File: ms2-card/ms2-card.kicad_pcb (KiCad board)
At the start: 2 copper layers, 100 x 54 mm, 40 parts, among them J1 Schaltregler, J10 MicroSD_SPI_CD, J11 I2C, J2 ESP Prog, J20 Smartcard Connector, J21 Card Edge, J23 Conn_01x04, J3 RTS, J30 USB_B_Micro, J31 Power Select, J32 FTDI Adapter, J40 SP1, J50 Conn_01x05, J51 SP1, Q30 BC847, SW1 RESET, U1 ESP-12F, U30 CH330N, U40 ADUM1250, U41 ADuM1201AR

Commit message: wip
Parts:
- removed C1: 100uF, Capacitor_Tantalum_SMD:CP_EIA-7343-31_Kemet-D_Pad2.25x2.55mm_HandSolder
- removed C30, C31, C40, C41, C50, C51: 100nF, Capacitors_SMD:C_0805_HandSoldering
- removed J1: Schaltregler, Connector_PinHeader_2.54mm:PinHeader_1x04_P2.54mm_Vertical
- removed J2: ESP Prog, Connector_PinHeader_2.54mm:PinHeader_1x02_P2.54mm_Vertical
- removed J3: RTS, Connector_PinHeader_2.54mm:PinHeader_1x01_P2.54mm_Vertical
- removed J31: Power Select, Connector_PinHeader_2.54mm:PinHeader_1x03_P2.54mm_Vertical
- removed J32: FTDI Adapter, Connector_PinSocket_2.54mm:PinSocket_1x06_P2.54mm_Horizontal
- removed J40, J51: SP1, Connector_PinHeader_2.54mm:PinHeader_1x01_P2.54mm_Vertical
- removed J50: Conn_01x05, Connector_PinHeader_2.54mm:PinHeader_1x05_P2.54mm_Vertical
- removed R2, R50, R51: 4k7, Resistors_SMD:R_0805_HandSolderingII
- removed U30: CH330N, Package_SO:SOIC-8_3.9x4.9mm_P1.27mm
- removed U40: ADUM1250, Package_SO:SOIC-8_3.9x4.9mm_P1.27mm
- removed U41: ADuM1201AR, Package_SO:SOIC-8_3.9x4.9mm_P1.27mm
- added Brd1: SSD1306, Lokkarten:128x64OLED, F.Cu at (173.4, 114.2)
- added J22: Card Edge, w_conn_misc:MS2_Edge, F.Cu at (104.2, 105.7)
- added M1: PI_PICO_ZERO, Lokkarten:PI_PICO_ZERO, F.Cu at (186.5, 142.6)
- J30: value USB_B_Micro -> Power Only
- R1: value 1k -> 330
- SW1: value RESET -> SW_Push
- U1: value ESP-12F -> W25Q128JVS; footprint ESP8266:ESP-12E -> Package_SO:SOIC-8_5.23x5.23mm_P1.27mm
- moved J11 49.3 mm to (172.8, 151.4), turned to 270 degrees
- moved D1 29.9 mm to (187.2, 130.2), turned to 180 degrees
- moved R1 25.8 mm to (180.7, 130.2)
- moved U1 20.4 mm to (171.0, 111.0), turned to 90 degrees
- moved J23 20.2 mm to (162.2, 133.2)
- moved J30 15.4 mm to (194.9, 127.1)
- moved R22 15.2 mm to (171.5, 131.5), turned to 0 degrees
- moved Q30 14.8 mm to (171.2, 125.3)
- moved R23 14.8 mm to (171.4, 128.7)
- moved R24 14.8 mm to (171.4, 122.1)
- moved R20 13.2 mm to (168.4, 144.4)
- moved R21 13.2 mm to (170.6, 144.4)
- moved SW1 10.1 mm to (167.5, 138.1), turned to 90 degrees
- moved J10 4.26 mm to (183.8, 113.2)
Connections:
- J10 pad 2: /CS -> /CS0
- J30 pad 1: /VBUS -> +5V
- SW1 pad 1: GND -> Net-(SW1-Pad1)
- U1 pad 1: Net-(SW1-Pad2) -> /CS1
- U1 pad 2: Net-(U1-Pad2) -> /MISO
- U1 pad 3: VCC -> Net-(U1-Pad3)
- U1 pad 4: /Card -> GND
- U1 pad 5: /CLK -> /MOSI
- U1 pad 6: /MISO -> /CLK
- U1 pad 7: /MOSI -> Net-(U1-Pad7)
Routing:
- net /SCL: track 155.3 -> 0.00 mm, vias 3 -> 0
- net VCC: track 150.9 -> 0.00 mm, vias 5 -> 0
- net /SDA: track 117.1 -> 0.00 mm, vias 2 -> 0
- net GND: track 89.6 -> 0.00 mm, vias 26 -> 0
- net Net-(J21-Pad1): track 71.5 -> 0.00 mm, vias 1 -> 0
- net /Card: track 69.6 -> 0.00 mm, vias 4 -> 0
- net /MS2PWR: track 62.2 -> 0.00 mm
- net Net-(J20-Pad2): track 61.2 -> 0.00 mm, vias 1 -> 0
- net Net-(J20-Pad4): track 52.8 -> 0.00 mm
- net Net-(J20-Pad7): track 45.8 -> 0.00 mm, vias 1 -> 0
- net /VBUS: track 44.8 -> 0.00 mm, vias 3 -> 0
- net Net-(J20-Pad5): track 44.0 -> 0.00 mm
- net /CS: track 40.3 -> 0.00 mm
- net Net-(SW1-Pad2): track 32.9 -> 0.00 mm
- net /MOSI: track 30.0 -> 0.00 mm, vias 1 -> 0
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- removed copper zone on B.Cu, net GND2
- removed copper zone on F.Cu, net GND2
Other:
- outline, holes or cut-outs redrawn
- board text added: "Lokkarten Emulator Gerhard Bertelsmann Hardi Stengelin 03/2022"
- board text removed: "3V3"
- board text removed: "5V"
- board text removed: "Lokkarten Emulator Hardi Stengelin Gerhard Bertelsmann 03/2022"
- board text removed: "MS2"
- board text removed: "RxD"
- board text removed: "TxD"
- board text removed: "USB"

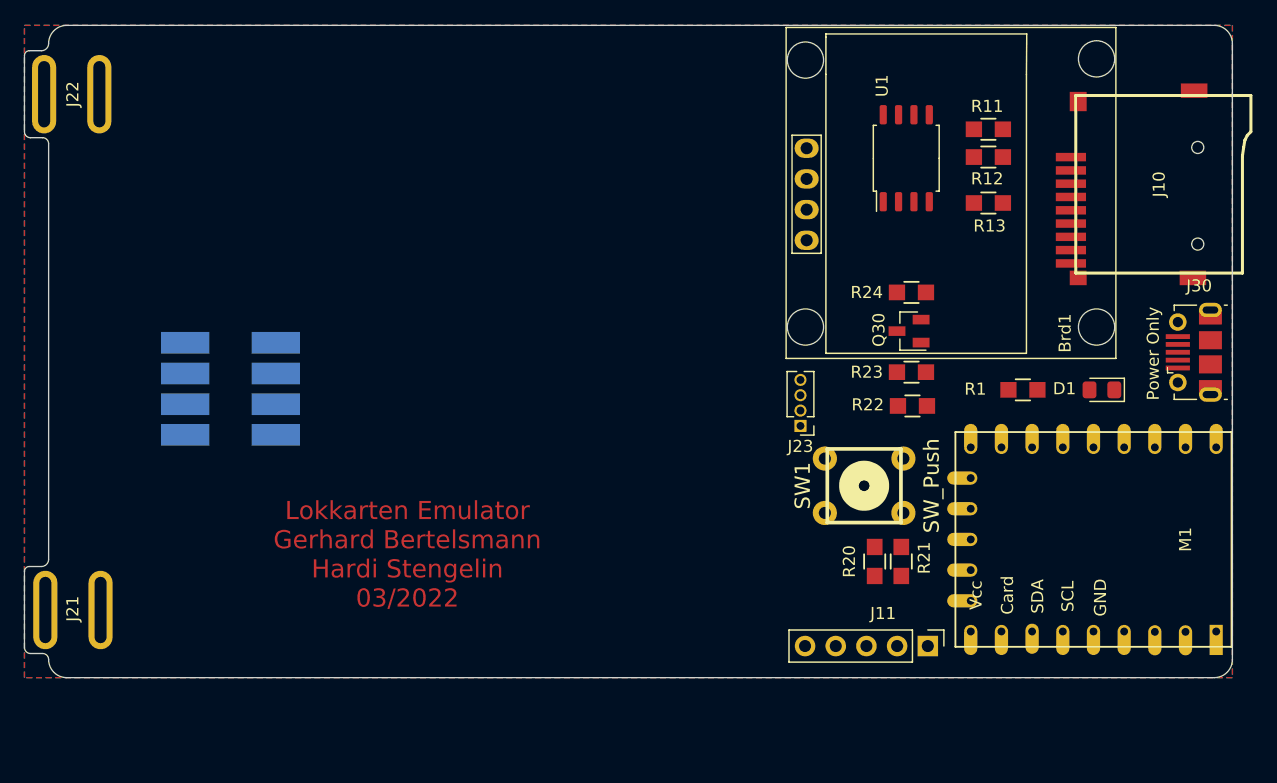
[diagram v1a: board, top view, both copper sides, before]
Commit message: new version with Pi Pico Zero
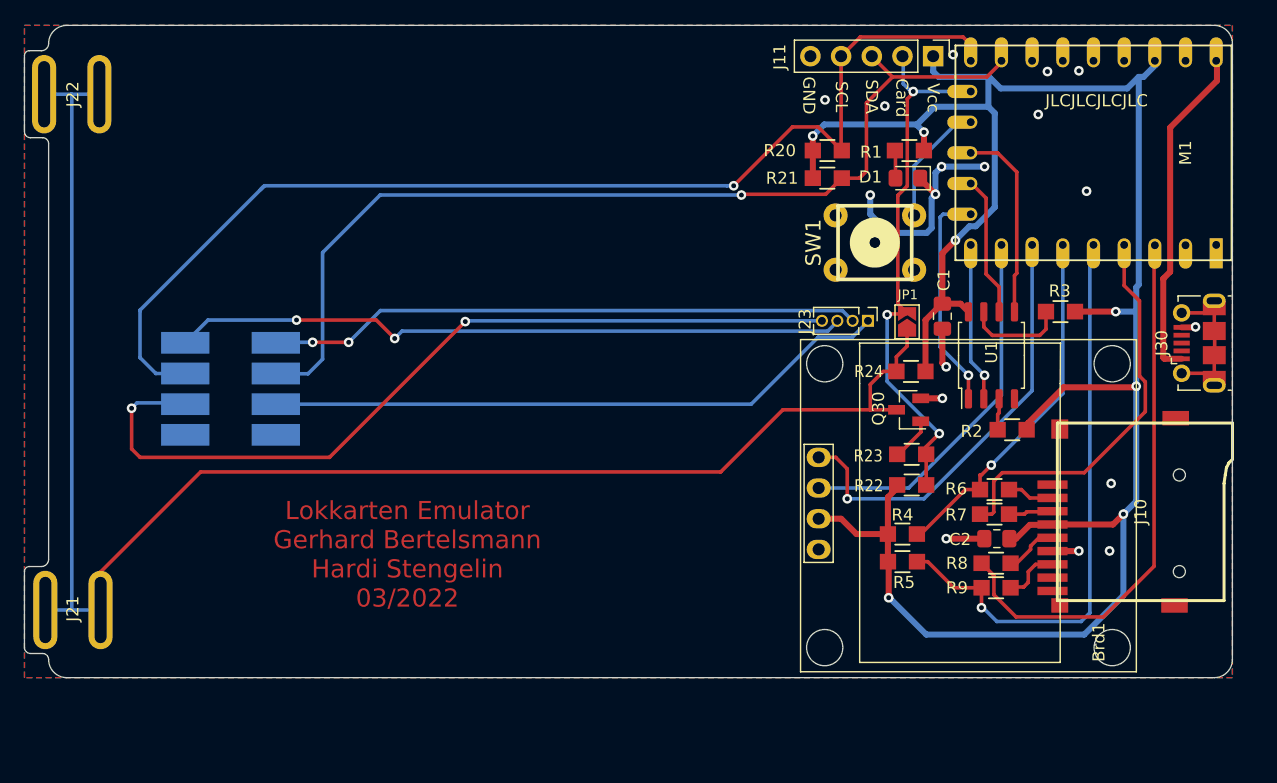
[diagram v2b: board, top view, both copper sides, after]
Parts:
- removed R11, R12, R13: 4k7, Resistors_SMD:R_0805_HandSolderingII
- added C1: 100nF, Capacitor_SMD:C_0805_2012Metric_Pad1.18x1.45mm_HandSolder, F.Cu at (174.0, 124.1)
- added C2: 100nF, Capacitor_SMD:C_0805_2012Metric_Pad1.18x1.45mm_HandSolder, F.Cu at (178.5, 142.5)
- added JP1: Jumper, Jumper:SolderJumper-2_P1.3mm_Open_TrianglePad1.0x1.5mm, F.Cu at (171.1, 124.5)
- added R2: 10k, Resistors_SMD:R_0805_HandSolderingII, F.Cu at (179.8, 133.5)
- added R3: 10k, Resistors_SMD:R_0805_HandSolderingII, F.Cu at (183.8, 123.7)
- added R4: 4k7, Resistors_SMD:R_0805_HandSolderingII, F.Cu at (170.7, 142.1)
- added R5: 4k7, Resistors_SMD:R_0805_HandSolderingII, F.Cu at (170.7, 144.4)
- added R6: 47, Resistors_SMD:R_0805_HandSolderingII, F.Cu at (178.3, 138.4)
- added R7: 47, Resistors_SMD:R_0805_HandSolderingII, F.Cu at (178.3, 140.5)
- added R8: 47, Resistors_SMD:R_0805_HandSolderingII, F.Cu at (178.4, 144.5)
- added R9: 47, Resistors_SMD:R_0805_HandSolderingII, F.Cu at (178.4, 146.6)
- moved J11 48.8 mm to (173.2, 102.6)
- moved R20 34.2 mm to (164.5, 110.4), turned to 0 degrees
- moved R21 32.3 mm to (164.5, 112.6), turned to 0 degrees
- moved M1 32.0 mm to (186.5, 110.6)
- moved J10 27.2 mm to (182.3, 140.3)
- moved Brd1 25.7 mm to (176.1, 139.8)
- moved D1 23.8 mm to (171.1, 112.6)
- moved R1 21.9 mm to (171.3, 110.4), turned to 180 degrees
- moved SW1 20.1 mm to (168.4, 118.0)
- moved U1 17.8 mm to (178.1, 127.3)
- moved J23 10.3 mm to (167.8, 124.5), turned to 270 degrees
- moved R23 6.80 mm to (171.4, 135.5)
- moved R22 6.54 mm to (171.4, 138.0)
- moved R24 6.54 mm to (171.4, 128.6)
- moved Q30 6.52 mm to (171.2, 131.8)
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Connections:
- net /MS2PWR renamed Net-(J20-Pad1)
- Brd1 pad 1: Net-(Brd1-Pad1) -> GND
- Brd1 pad 2: Net-(Brd1-Pad2) -> VCC
- Brd1 pad 3: Net-(Brd1-Pad3) -> /SCL1
- Brd1 pad 4: Net-(Brd1-Pad4) -> /SDA1
- J10 pad 2: /CS0 -> Net-(J10-Pad2)
- J10 pad 3: /MOSI -> Net-(J10-Pad3)
- J10 pad 5: /CLK -> Net-(J10-Pad5)
- J10 pad 7: /MISO -> Net-(J10-Pad7)
- J11 pad 3: /SDA -> /SDA0
- J11 pad 4: /SCL -> /SCL0
- J20 pad 3: /SCL -> /SCL0
- J20 pad 6: /SDA -> /SDA0
- M1 pad 10: Net-(M1-Pad10) -> /CLK1
- M1 pad 11: Net-(M1-Pad11) -> /MOSI1
- M1 pad 12: Net-(M1-Pad12) -> /GP12
- M1 pad 13: Net-(M1-Pad13) -> /Card
- M1 pad 14: Net-(M1-Pad14) -> /SCL0
- M1 pad 15: Net-(M1-Pad15) -> /SDA0
- M1 pad 2: Net-(M1-Pad2) -> /CLK0
- M1 pad 3: Net-(M1-Pad3) -> /MOSI0
- M1 pad 30: Net-(M1-Pad30) -> VCC
- M1 pad 31: Net-(M1-Pad31) -> GND
- M1 pad 32: Net-(M1-Pad32) -> +5V
- M1 pad 4: Net-(M1-Pad4) -> /MISO0
- M1 pad 5: Net-(M1-Pad5) -> /CS0
- M1 pad 6: Net-(M1-Pad6) -> /SDA1
- M1 pad 7: Net-(M1-Pad7) -> /SCL1
- M1 pad 8: Net-(M1-Pad8) -> /MISO1
- M1 pad 9: Net-(M1-Pad9) -> /CS1
- R20 pad 2: /SCL -> /SCL0
- R21 pad 2: /SDA -> /SDA0
- SW1 pad 1: Net-(SW1-Pad1) -> GND
- SW1 pad 2: Net-(SW1-Pad2) -> /GP12
- U1 pad 2: /MISO -> /MISO1
- U1 pad 5: /MOSI -> /MOSI1
- U1 pad 6: /CLK -> /CLK1
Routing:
- net VCC: track 0.00 -> 179.6 mm, vias 0 -> 7
- net Net-(J21-Pad1): track 0.00 -> 134.4 mm
- net /SCL0: track 0.00 -> 94.7 mm, vias 0 -> 1
- net /SDA0: track 0.00 -> 81.6 mm, vias 0 -> 1
- net Net-(J20-Pad2): track 0.00 -> 70.3 mm, vias 0 -> 2
- net Net-(J20-Pad4): track 0.00 -> 56.0 mm, vias 0 -> 2
- net Net-(J20-Pad7): track 0.00 -> 51.9 mm
- net Net-(J20-Pad5): track 0.00 -> 49.2 mm, vias 0 -> 2
- net /MISO0: track 0.00 -> 48.2 mm, vias 0 -> 1
- net /CLK0: track 0.00 -> 45.4 mm
- net /Card: track 0.00 -> 45.3 mm, vias 0 -> 3
- net /SDA1: track 0.00 -> 36.3 mm, vias 0 -> 1
- net /MOSI0: track 0.00 -> 33.5 mm
- net /SCL1: track 0.00 -> 30.7 mm
- net /CS0: track 0.00 -> 29.9 mm, vias 0 -> 1
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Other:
- board text added: "JLCJLCJLCJLC"

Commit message: fix schematic
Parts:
- J30: value Power Only -> Power_Only
- R2, R3: value 10k -> 4k7
- moved C2 0.13 mm to (178.4, 142.5)
- moved R8 0.13 mm to (178.3, 144.5), turned to 0 degrees
- moved R9 0.13 mm to (178.3, 146.6), turned to 0 degrees
- moved R4 0.06 mm to (170.7, 142.2)
- moved J30 0.06 mm to (195.3, 126.3)
- turned R6 to 0 degrees
- turned R7 to 0 degrees
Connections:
- R6 pad 1: Net-(J10-Pad2) -> /CS0
- R6 pad 2: /CS0 -> Net-(J10-Pad2)
- R7 pad 1: Net-(J10-Pad3) -> /MOSI0
- R7 pad 2: /MOSI0 -> Net-(J10-Pad3)
- R8 pad 1: Net-(J10-Pad5) -> /CLK0
- R8 pad 2: /CLK0 -> Net-(J10-Pad5)
- R9 pad 1: Net-(J10-Pad7) -> /MISO0
- R9 pad 2: /MISO0 -> Net-(J10-Pad7)
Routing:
- net GND: track 29.9 -> 36.2 mm, vias 14 -> 15
